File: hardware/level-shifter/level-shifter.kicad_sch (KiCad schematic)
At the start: 41 parts, among them J1 Conn_01x10_Socket, J2 Conn_01x10_Socket, J3 Conn_01x10_Socket, J4 Conn_01x10_Socket, J5 Conn_01x10_Pin, J6 Conn_01x10_Pin, J7 Conn_01x10_Pin, J8 Conn_01x10_Pin, J9 USB_C_Receptacle_USB2.0_16P, U11 TLV75533PDBV

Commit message: start of devhat redo
remove usb stuff because the devboard supplies 3.3v
pinout of devboard was wackier than previously thought
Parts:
- removed C1, C2, C7: 10u 10V, Capacitor_SMD:C_0603_1608Metric, symbol Device:C_Small
- removed C3, C4: 100n 20V, Capacitor_SMD:C_0805_2012Metric, symbol Device:C_Small
- removed C5: 100n 16V, Capacitor_SMD:C_0603_1608Metric, symbol Device:C_Small
- removed C6: 1u 10V, Capacitor_SMD:C_0805_2012Metric, symbol Device:C_Small
- removed C8: 10u >= 5V, Capacitor_SMD:C_0603_1608Metric, symbol Device:C_Small
- removed FB1: 25% 220 2.2A, Capacitor_SMD:C_0603_1608Metric, symbol Device:FerriteBead_Small
- removed J1, J2, J3, J4: Conn_01x10_Socket, Connector_PinHeader_2.54mm:PinHeader_1x10_P2.54mm_Vertical, symbol Connector:Conn_01x10_Socket
- removed J5, J6, J7, J8: Conn_01x10_Pin, Connector_PinHeader_2.54mm:PinHeader_1x10_P2.54mm_Vertical, symbol Connector:Conn_01x10_Pin
- removed J9: USB_C_Receptacle_USB2.0_16P, Connector_USB:USB_C_Receptacle_GCT_USB4110, symbol Connector:USB_C_Receptacle_USB2.0_16P
- removed R11, R12: 1% 5.1k 0.063W, Resistor_SMD:R_0402_1005Metric, symbol Device:R_Small
- removed U11: TLV75533PDBV, Package_TO_SOT_SMD:SOT-23-5, symbol Regulator_Linear:TLV75533PDBV
- added J1, J4: Conn_02x24_Odd_Even, Connector_PinHeader_2.54mm:PinHeader_2x24_P2.54mm_Vertical, symbol Connector_Generic:Conn_02x24_Odd_Even
- added J2, J3: Conn_01x20_Pin, Connector_PinHeader_2.54mm:PinHeader_1x20_P2.54mm_Vertical, symbol Connector:Conn_01x20_Pin
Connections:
- net +3V3: now also R10.1, R6.1, R7.1, R8.1, R9.1, U10.1 (VCC_A), U6.1 (VCC_A), U7.1 (VCC_A), U8.1 (VCC_A), U9.1 (VCC_A), J1.2 (Pin_2), J1.45 (Pin_45), J4.1 (Pin_1), J4.47 (Pin_47), J4.48 (Pin_48); no longer U10.12 (VCC_B), U6.12 (VCC_B), U7.12 (VCC_B), U8.12 (VCC_B), U9.12 (VCC_B)
- net +5V: now also U10.12 (VCC_B), U6.12 (VCC_B), U7.12 (VCC_B), U8.12 (VCC_B), U9.12 (VCC_B), J2.11 (Pin_11); no longer R10.1, R6.1, R7.1, R8.1, R9.1, U10.1 (VCC_A), U6.1 (VCC_A), U7.1 (VCC_A), U8.1 (VCC_A), U9.1 (VCC_A)
- net A0_5V: now also U8.9 (B3), J3.11 (Pin_11); no longer U8.4 (A3)
- net A0_FPGA: now also U8.2 (A1), J4.31 (Pin_31); no longer U8.9 (B3)
- net A10_5V: now also U6.11 (B1), J3.1 (Pin_1); no longer U6.2 (A1)
- net A10_FPGA: now also U6.2 (A1), J4.3 (Pin_3); no longer U6.11 (B1)
- net A11_5V: now also J2.1 (Pin_1)
- net A11_FPGA: now also J1.4 (Pin_4)
- net A12_5V: now also J2.2 (Pin_2)
- net A12_FPGA: now also J1.3 (Pin_3)
- net A13_5V: now also J2.3 (Pin_3)
- net A13_FPGA: now also J1.6 (Pin_6)
- net A14_5V: now also J2.4 (Pin_4)
- net A14_FPGA: now also J1.5 (Pin_5)
- net A15_5V: now also J2.5 (Pin_5)
- net A15_FPGA: now also J1.8 (Pin_8)
- net A1_5V: now also U8.10 (B2), J3.10 (Pin_10); no longer U8.3 (A2)
- net A1_FPGA: now also U8.3 (A2), J4.12 (Pin_12); no longer U8.10 (B2)
- net A2_5V: now also U8.11 (B1), J3.9 (Pin_9); no longer U8.2 (A1)
- net A2_FPGA: now also U8.4 (A3), J4.11 (Pin_11); no longer U8.11 (B1)
- net A3_5V: now also U7.8 (B4), J3.8 (Pin_8); no longer U7.5 (A4)
- net A3_FPGA: now also U7.5 (A4), J4.10 (Pin_10); no longer U7.8 (B4)
- net A4_5V: now also U7.9 (B3), J3.7 (Pin_7); no longer U7.4 (A3)
- net A4_FPGA: now also U7.4 (A3), J4.9 (Pin_9); no longer U7.9 (B3)
- net A5_5V: now also U7.10 (B2), J3.6 (Pin_6); no longer U7.3 (A2)
- net A5_FPGA: now also U7.3 (A2), J4.8 (Pin_8); no longer U7.10 (B2)
- net A6_5V: now also U7.11 (B1), J3.5 (Pin_5); no longer U7.2 (A1)
- net A6_FPGA: now also U7.2 (A1), J4.7 (Pin_7); no longer U7.11 (B1)
- net A7_5V: now also U6.8 (B4), J3.4 (Pin_4); no longer U6.5 (A4)
- net A7_FPGA: now also U6.5 (A4), J4.6 (Pin_6); no longer U6.8 (B4)
- net A8_5V: now also U6.9 (B3), J3.3 (Pin_3); no longer U6.4 (A3)
- net A8_FPGA: now also U6.4 (A3), J4.5 (Pin_5); no longer U6.9 (B3)
- net A9_5V: now also U6.10 (B2), J3.2 (Pin_2); no longer U6.3 (A2)
- net A9_FPGA: now also U6.3 (A2), J4.4 (Pin_4); no longer U6.10 (B2)
- net BUSAK_5V: now also U10.10 (B2), J3.18 (Pin_18); no longer U10.3 (A2)
- net BUSAK_FPGA: now also U10.3 (A2), J4.41 (Pin_41); no longer U10.10 (B2)
- net BUSRQ_5V: now also U9.8 (B4), J3.16 (Pin_16); no longer U9.5 (A4)
- net BUSRQ_FPGA: now also U9.5 (A4), J4.39 (Pin_39); no longer U9.8 (B4)
- net CLK: now also J1.7 (Pin_7)
- net CLK_5V: now also J2.6 (Pin_6)
- net D0_5V: now also J2.14 (Pin_14)
- net D0_FPGA: now also J1.32 (Pin_32)
- net D1_5V: now also J2.15 (Pin_15)
- net D1_FPGA: now also J1.34 (Pin_34)
- net D2_5V: now also J2.12 (Pin_12)
- net D2_FPGA: now also J1.30 (Pin_30)
- net D3_5V: now also J2.8 (Pin_8)
- net D3_FPGA: now also J1.9 (Pin_9)
- net D4_5V: now also J2.7 (Pin_7)
- net D4_FPGA: now also J1.10 (Pin_10)
- net D5_5V: now also J2.9 (Pin_9)
- net D5_FPGA: now also J1.12 (Pin_12)
- net D6_5V: now also J2.10 (Pin_10)
- net D6_FPGA: now also J1.11 (Pin_11)
- net D7_5V: now also J2.13 (Pin_13)
- net D7_FPGA: now also J1.31 (Pin_31)
- net GND: now also J1.1 (Pin_1), J1.23 (Pin_23), J1.24 (Pin_24), J1.25 (Pin_25), J1.26 (Pin_26), J1.47 (Pin_47), J1.48 (Pin_48), J3.12 (Pin_12), J4.2 (Pin_2), J4.25 (Pin_25), J4.26 (Pin_26), J4.45 (Pin_45), J4.46 (Pin_46)
- net HALT_5V: now also J2.18 (Pin_18)
- net HALT_FPGA: now also J1.35 (Pin_35)
- net INT_5V: now also J2.16 (Pin_16)
- net INT_FPGA: now also J1.33 (Pin_33)
- net IORQ_5V: now also J2.20 (Pin_20)
- net IORQ_FPGA: now also J1.37 (Pin_37)
- net M1_5V: now also U9.10 (B2), J3.14 (Pin_14); no longer U9.3 (A2)
- net M1_FPGA: now also U9.3 (A2), J4.35 (Pin_35); no longer U9.10 (B2)
- net MREQ_5V: now also J2.19 (Pin_19)
- net MREQ_FPGA: now also J1.38 (Pin_38)
- net NMI_5V: now also J2.17 (Pin_17)
- net NMI_FPGA: now also J1.36 (Pin_36)
- net RD_5V: now also U10.8 (B4), J3.20 (Pin_20); no longer U10.5 (A4)
- net RD_FPGA: now also U10.5 (A4), J4.43 (Pin_43); no longer U10.8 (B4)
- net RESET_5V: now also U9.9 (B3), J3.15 (Pin_15); no longer U9.4 (A3)
- net RESET_FPGA: now also U9.4 (A3), J4.40 (Pin_40); no longer U9.9 (B3)
- net RFSH_5V: now also U9.11 (B1), J3.13 (Pin_13); no longer U9.2 (A1)
- net RFSH_FPGA: now also U9.2 (A1), J4.36 (Pin_36); no longer U9.11 (B1)
- net WAIT_5V: now also U10.11 (B1), J3.17 (Pin_17); no longer U10.2 (A1)
- net WAIT_FPGA: now also U10.2 (A1), J4.42 (Pin_42); no longer U10.11 (B1)
- net WR_5V: now also U10.9 (B3), J3.19 (Pin_19); no longer U10.4 (A3)
- net WR_FPGA: now also U10.4 (A3), J4.44 (Pin_44); no longer U10.9 (B3)
- no-connect marks 12 -> 45
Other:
- note added: "Narvi S7 will be upside down!!! (bottom facing up) micro USB on this end"
- note added: "P4"
- note added: "P4 A"
- note added: "P4 B"
- note added: "P5"
- note added: "P5 C"
- note added: "P5 D"
- note added: "image has been mirrored to show orientation when upside down"
- note added: "z80 DIP :)"
- note removed: "Connectors for side 1"
- note removed: "Connectors for side 2"
- note removed: "Ferrite bead 0603"

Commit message: devhat redo "done"
NO PEEKING AT THE BOARD UNTIL THE REVEAL!!!
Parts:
- removed U1, U10, U2, U3, U4, U5, U6, U7, U8, U9: ~, hardware:NXB0104_XQFN12, symbol custom_symbols:NXB0104_XQFN12
- added IC1, IC10, IC2, IC3, IC4, IC5, IC6, IC7, IC8, IC9: NXB0104PW-Q100J, hardware:SOP65P640X110-14N, symbol NXB0104PW-Q100J:NXB0104PW-Q100J
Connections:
- net +3V3: now also IC1.1 (VCC(A)), IC10.1 (VCC(A)), IC2.1 (VCC(A)), IC3.1 (VCC(A)), IC4.1 (VCC(A)), IC5.1 (VCC(A)), IC6.1 (VCC(A)), IC7.1 (VCC(A)), IC8.1 (VCC(A)), IC9.1 (VCC(A))
- net +5V: now also IC1.14 (VCC(B)), IC10.14 (VCC(B)), IC2.14 (VCC(B)), IC3.14 (VCC(B)), IC4.14 (VCC(B)), IC5.14 (VCC(B)), IC6.14 (VCC(B)), IC7.14 (VCC(B)), IC8.14 (VCC(B)), IC9.14 (VCC(B))
- net A0_5V: now also IC8.11 (B3)
- net A0_FPGA: now also IC8.2 (A1)
- net A10_5V: now also IC6.13 (B1)
- net A10_FPGA: now also J4.6 (Pin_6), IC6.2 (A1); no longer J4.3 (Pin_3)
- net A11_5V: now also IC1.13 (B1)
- net A11_FPGA: now also IC1.2 (A1)
- net A12_5V: now also IC1.12 (B2)
- net A12_FPGA: now also IC1.3 (A2)
- net A13_5V: now also IC1.11 (B3)
- net A13_FPGA: now also IC1.4 (A3)
- net A14_5V: now also IC1.10 (B4)
- net A14_FPGA: now also IC1.5 (A4)
- net A15_5V: now also IC2.13 (B1)
- net A15_FPGA: now also J1.14 (Pin_14), IC2.2 (A1); no longer J1.8 (Pin_8)
- net A1_5V: now also IC8.12 (B2)
- net A1_FPGA: now also J4.32 (Pin_32), IC8.3 (A2); no longer J4.12 (Pin_12)
- net A2_5V: now also IC8.13 (B1)
- net A2_FPGA: now also J4.29 (Pin_29), IC8.4 (A3); no longer J4.11 (Pin_11)
- net A3_5V: now also IC7.10 (B4)
- net A3_FPGA: now also J4.13 (Pin_13), IC7.5 (A4); no longer J4.10 (Pin_10)
- net A4_5V: now also IC7.11 (B3)
- net A4_FPGA: now also J4.14 (Pin_14), IC7.4 (A3); no longer J4.9 (Pin_9)
- net A5_5V: now also IC7.12 (B2)
- net A5_FPGA: now also J4.15 (Pin_15), IC7.3 (A2); no longer J4.8 (Pin_8)
- net A6_5V: now also IC7.13 (B1)
- net A6_FPGA: now also J4.16 (Pin_16), IC7.2 (A1); no longer J4.7 (Pin_7)
- net A7_5V: now also IC6.10 (B4)
- net A7_FPGA: now also J4.3 (Pin_3), IC6.5 (A4); no longer J4.6 (Pin_6)
- net A8_5V: now also IC6.11 (B3)
- net A8_FPGA: now also J4.4 (Pin_4), IC6.4 (A3); no longer J4.5 (Pin_5)
- net A9_5V: now also IC6.12 (B2)
- net A9_FPGA: now also J4.5 (Pin_5), IC6.3 (A2); no longer J4.4 (Pin_4)
- net BUSAK_5V: now also IC10.12 (B2)
- net BUSAK_FPGA: now also J4.43 (Pin_43), IC10.3 (A2); no longer J4.41 (Pin_41)
- net BUSRQ_5V: now also IC9.10 (B4)
- net BUSRQ_FPGA: now also J4.36 (Pin_36), IC9.5 (A4); no longer J4.39 (Pin_39)
- net CLK: now also J1.13 (Pin_13), IC2.3 (A2); no longer J1.7 (Pin_7)
- net CLK_5V: now also IC2.12 (B2)
- net D0_5V: now also IC4.12 (B2)
- net D0_FPGA: now also J1.31 (Pin_31), IC4.3 (A2); no longer J1.32 (Pin_32)
- net D1_5V: now also IC4.11 (B3)
- net D1_FPGA: now also IC4.4 (A3)
- net D2_5V: now also IC3.10 (B4)
- net D2_FPGA: now also J1.28 (Pin_28), IC3.5 (A4); no longer J1.30 (Pin_30)
- net D3_5V: now also IC2.10 (B4)
- net D3_FPGA: now also J1.15 (Pin_15), IC2.5 (A4); no longer J1.9 (Pin_9)
- net D4_5V: now also IC2.11 (B3)
- net D4_FPGA: now also J1.16 (Pin_16), IC2.4 (A3); no longer J1.10 (Pin_10)
- net D5_5V: now also IC3.13 (B1)
- net D5_FPGA: now also J1.22 (Pin_22), IC3.2 (A1); no longer J1.12 (Pin_12)
- net D6_5V: now also IC3.12 (B2)
- net D6_FPGA: now also J1.21 (Pin_21), IC3.3 (A2); no longer J1.11 (Pin_11)
- net D7_5V: now also IC4.13 (B1)
- net D7_FPGA: now also J1.32 (Pin_32), IC4.2 (A1); no longer J1.31 (Pin_31)
- net GND: now also IC1.7 (GND), IC10.7 (GND), IC2.7 (GND), IC3.7 (GND), IC4.7 (GND), IC5.7 (GND), IC6.7 (GND), IC7.7 (GND), IC8.7 (GND), IC9.7 (GND)
- net HALT_5V: now also IC5.12 (B2)
- net HALT_FPGA: now also IC5.3 (A2)
- net INT_5V: now also IC4.10 (B4)
- net INT_FPGA: now also IC4.5 (A4)
- net IORQ_5V: now also IC5.10 (B4)
- net IORQ_FPGA: now also IC5.5 (A4)
- net M1_5V: now also IC9.12 (B2)
- net M1_FPGA: now also J4.39 (Pin_39), IC9.3 (A2); no longer J4.35 (Pin_35)
- net MREQ_5V: now also IC5.11 (B3)
- net MREQ_FPGA: now also IC5.4 (A3)
- net NMI_5V: now also IC5.13 (B1)
- net NMI_FPGA: now also IC5.2 (A1)
- net RD_5V: now also IC10.10 (B4)
- net RD_FPGA: now also J4.41 (Pin_41), IC10.5 (A4); no longer J4.43 (Pin_43)
- net RESET_5V: now also IC9.11 (B3)
- net RESET_FPGA: now also J4.35 (Pin_35), IC9.4 (A3); no longer J4.40 (Pin_40)
- net RFSH_5V: now also IC9.13 (B1)
- net RFSH_FPGA: now also J4.40 (Pin_40), IC9.2 (A1); no longer J4.36 (Pin_36)
- net WAIT_5V: now also IC10.13 (B1)
- net WAIT_FPGA: now also J4.44 (Pin_44), IC10.2 (A1); no longer J4.42 (Pin_42)
- net WR_5V: now also IC10.11 (B3)
- net WR_FPGA: now also J4.42 (Pin_42), IC10.4 (A3); no longer J4.44 (Pin_44)
- net at R5.2: now also IC5.8 (OE)
- net at R9.2: now also IC9.8 (OE)
- net at R7.2: now also IC7.8 (OE)
- net at R8.2: now also IC8.8 (OE)
- net at R4.2: now also IC4.8 (OE)
- net at R1.2: now also IC1.8 (OE)
- net at R10.2: now also IC10.8 (OE)
- net at R6.2: now also IC6.8 (OE)
- net at R3.2: now also IC3.8 (OE)
- net at R2.2: now also IC2.8 (OE)
- no-connect marks 45 -> 65
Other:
- note added: "Z80 System <-> Translation Board <-> FPGA Board Connectors"
- note removed: "USB-C 5V->3V3 Power Supply from host PC"
- note removed: "Z80 System <-> Translation Board Connectors"
- moved on the sheet: R1, R2, R3, R4, R5, R8

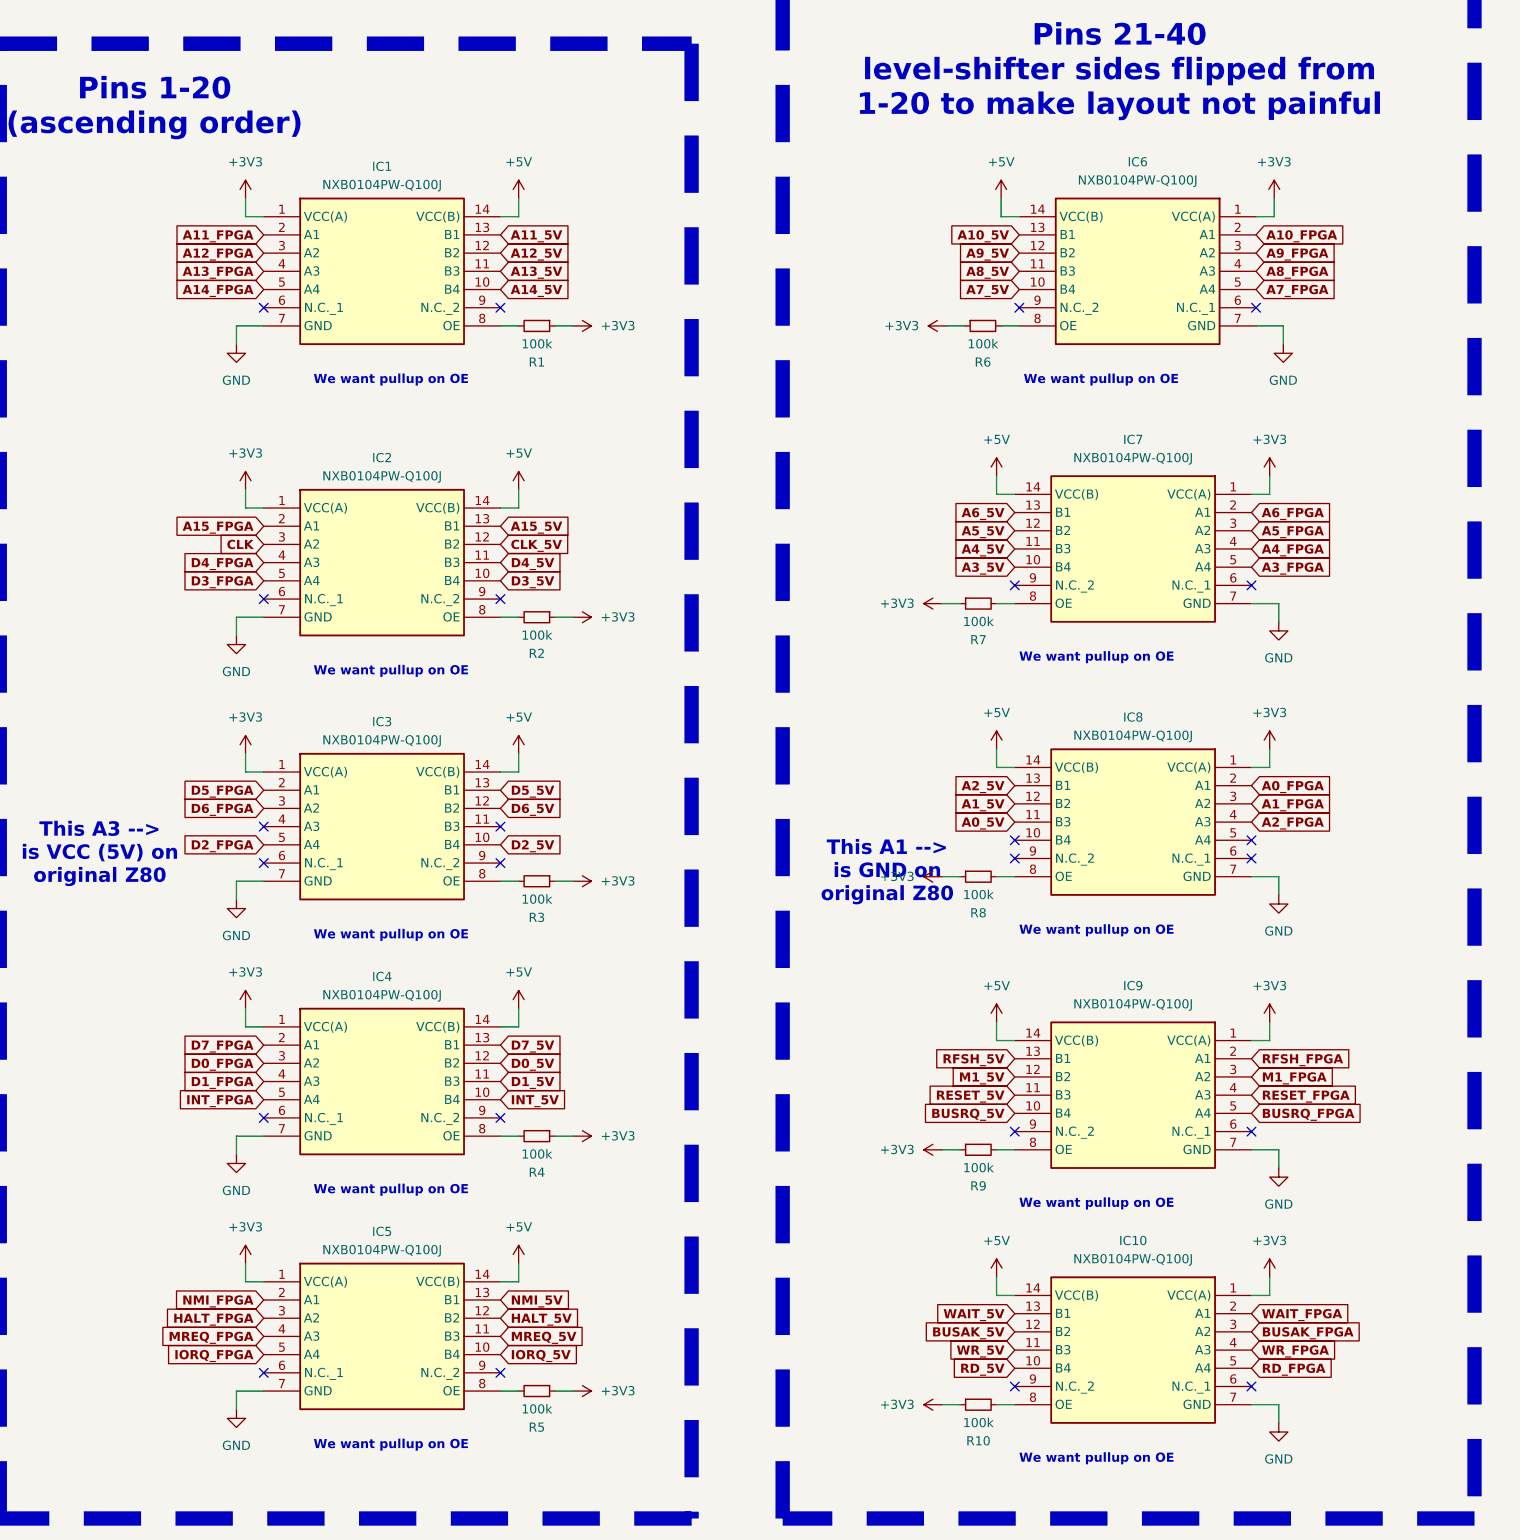
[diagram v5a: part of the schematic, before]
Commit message: added decoupling caps to level shifters
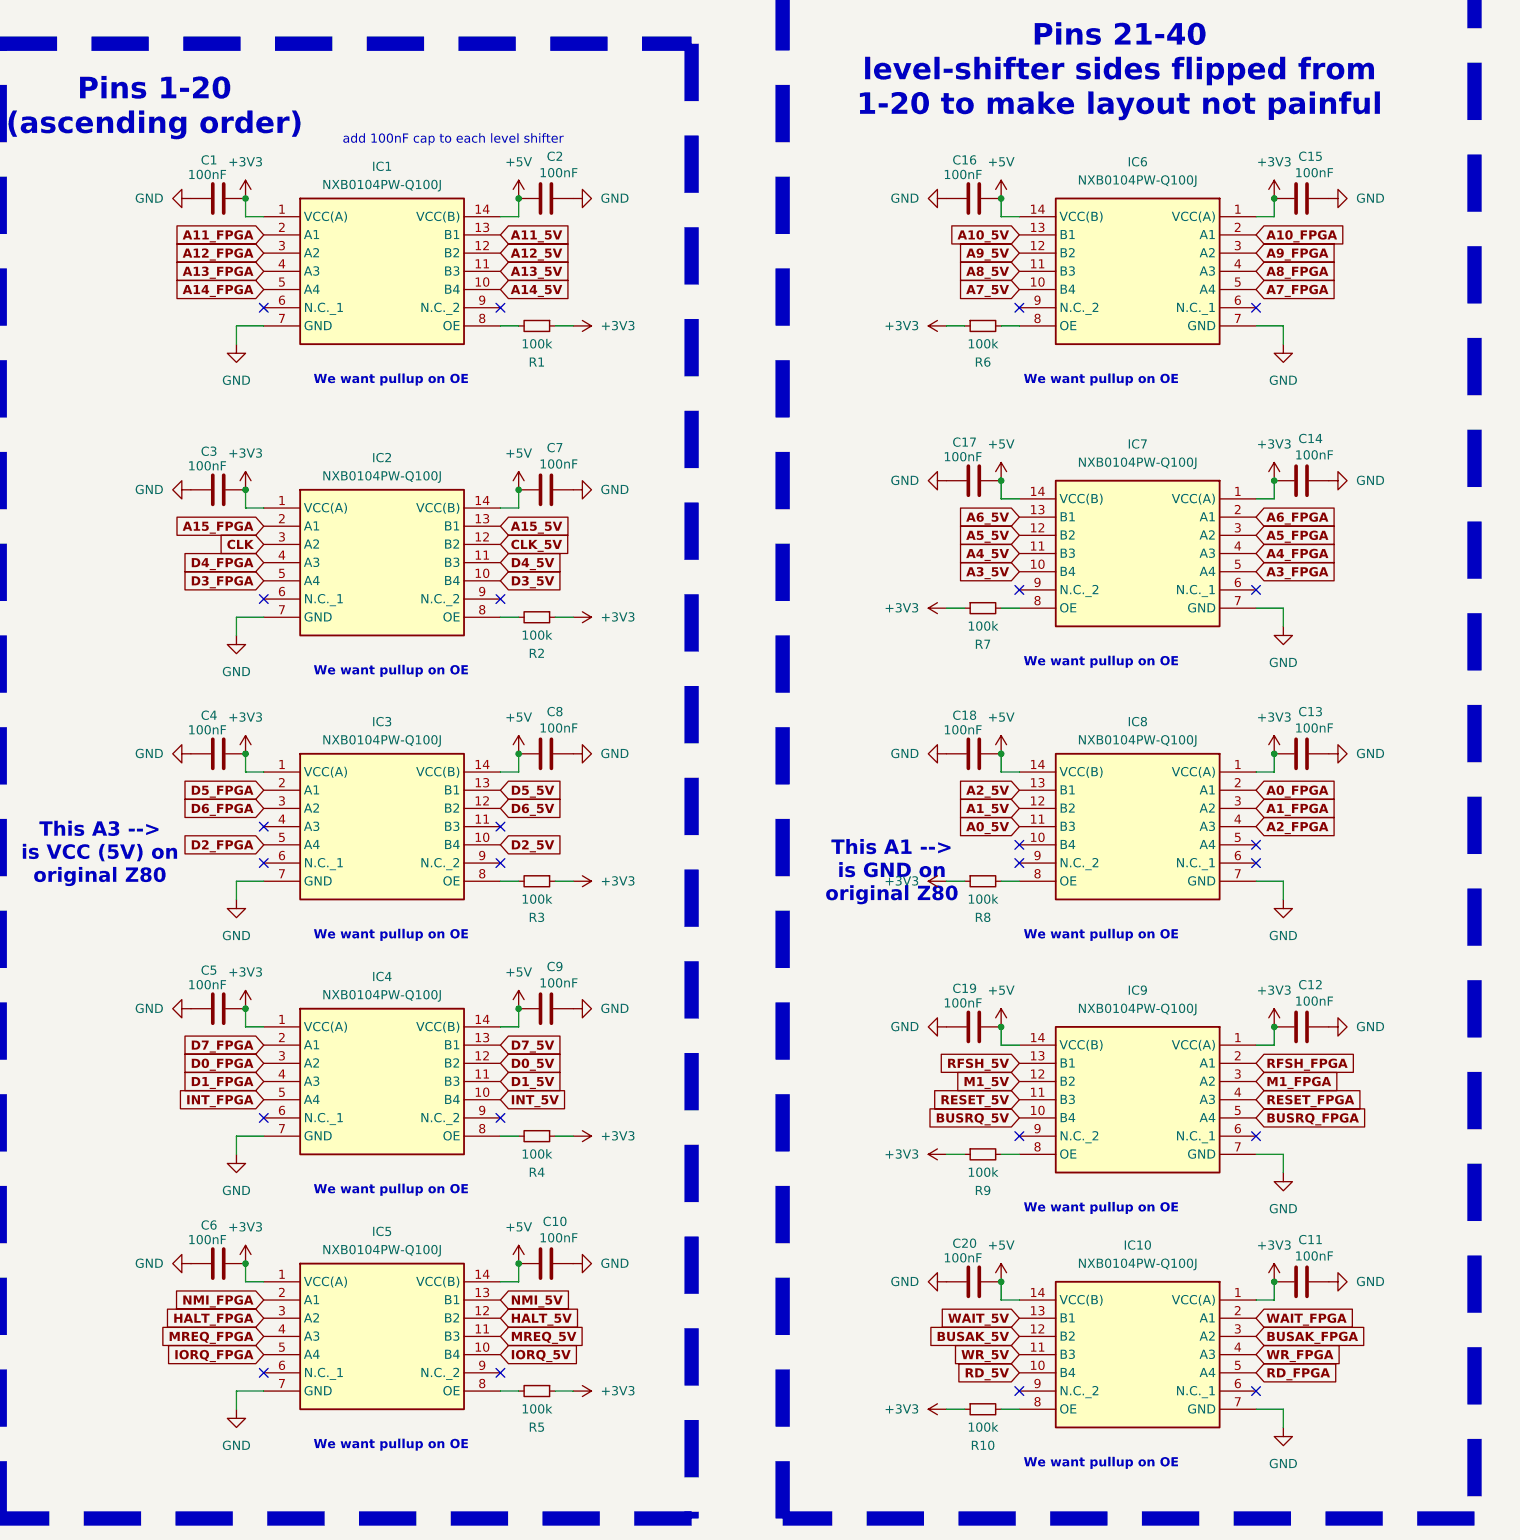
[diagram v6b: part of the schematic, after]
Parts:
- added C1, C10, C11, C12, C13, C14, C15, C16, C17, C18, C19, C2, C20, C3, C4, C5, C6, C7, C8, C9: 100nF, symbol Device:C
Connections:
- net +3V3: now also C1.2, C11.1, C12.1, C13.1, C14.1, C15.1, C3.2, C4.2, C5.2, C6.2
- net +5V: now also C10.1, C16.2, C17.2, C18.2, C19.2, C2.1, C20.2, C7.1, C8.1, C9.1
- net GND: now also C1.1, C10.2, C11.2, C12.2, C13.2, C14.2, C15.2, C16.1, C17.1, C18.1, C19.1, C2.2, C20.1, C3.1, C4.1, C5.1, C6.1, C7.2, C8.2, C9.2
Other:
- note added: "add 100nF cap to each level shifter"
- moved on the sheet: IC10, IC7, IC8, IC9, R10, R7, R8, R9
